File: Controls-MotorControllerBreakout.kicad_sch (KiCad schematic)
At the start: 15 parts, among them J1 MC CAN 1, J2 MC CAN 2, J3 CAN INTRFC, J4 EXT PWR

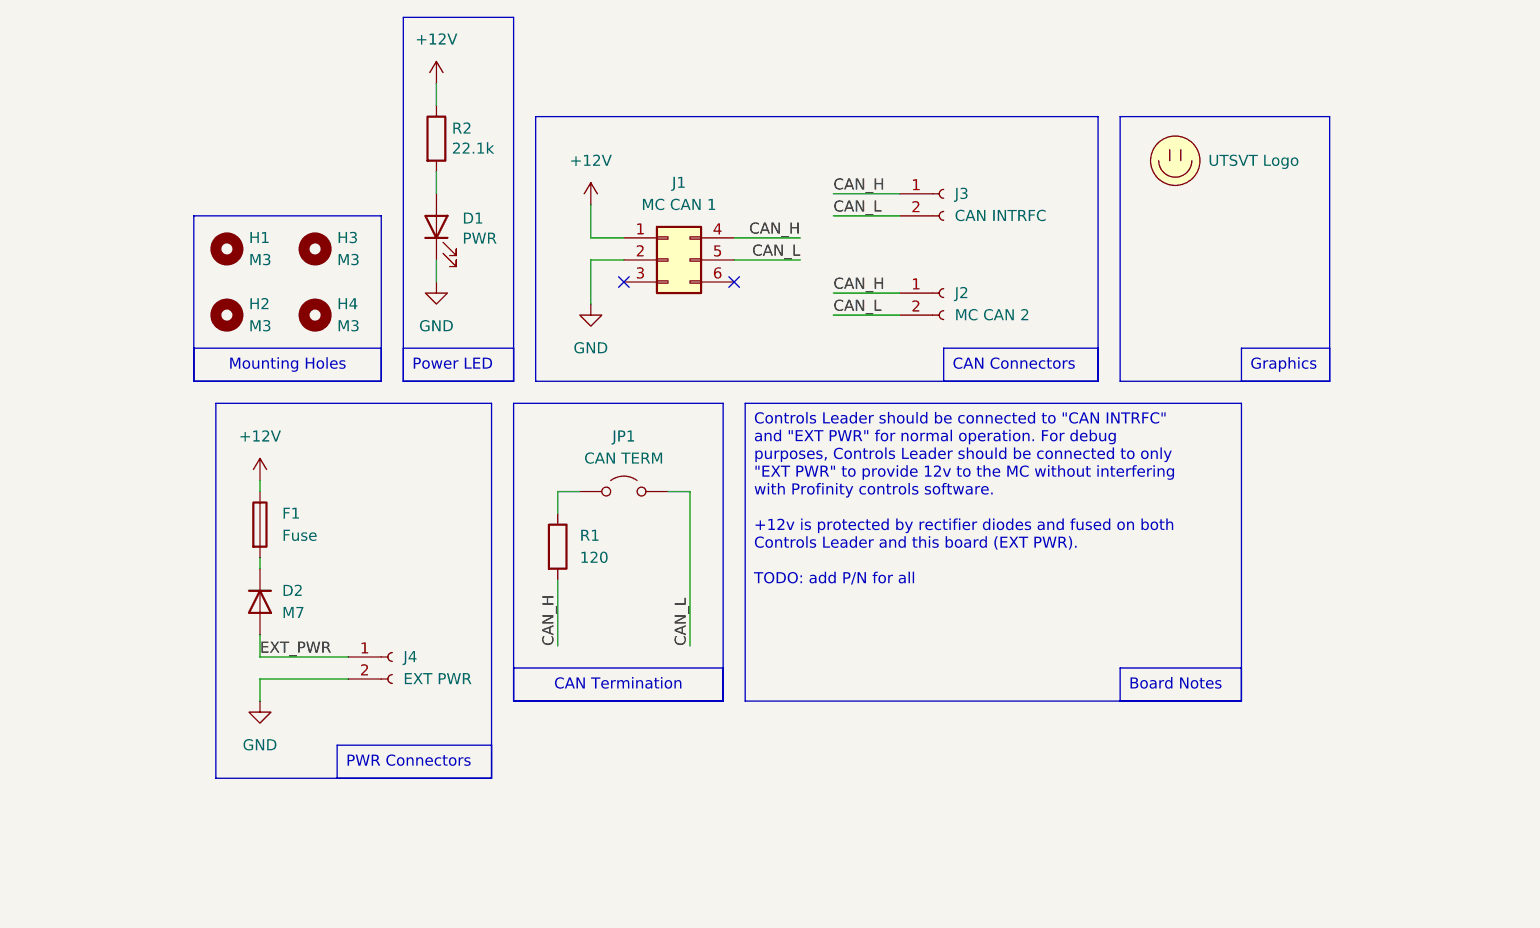
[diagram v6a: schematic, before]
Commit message: fix PP & add dsub conn
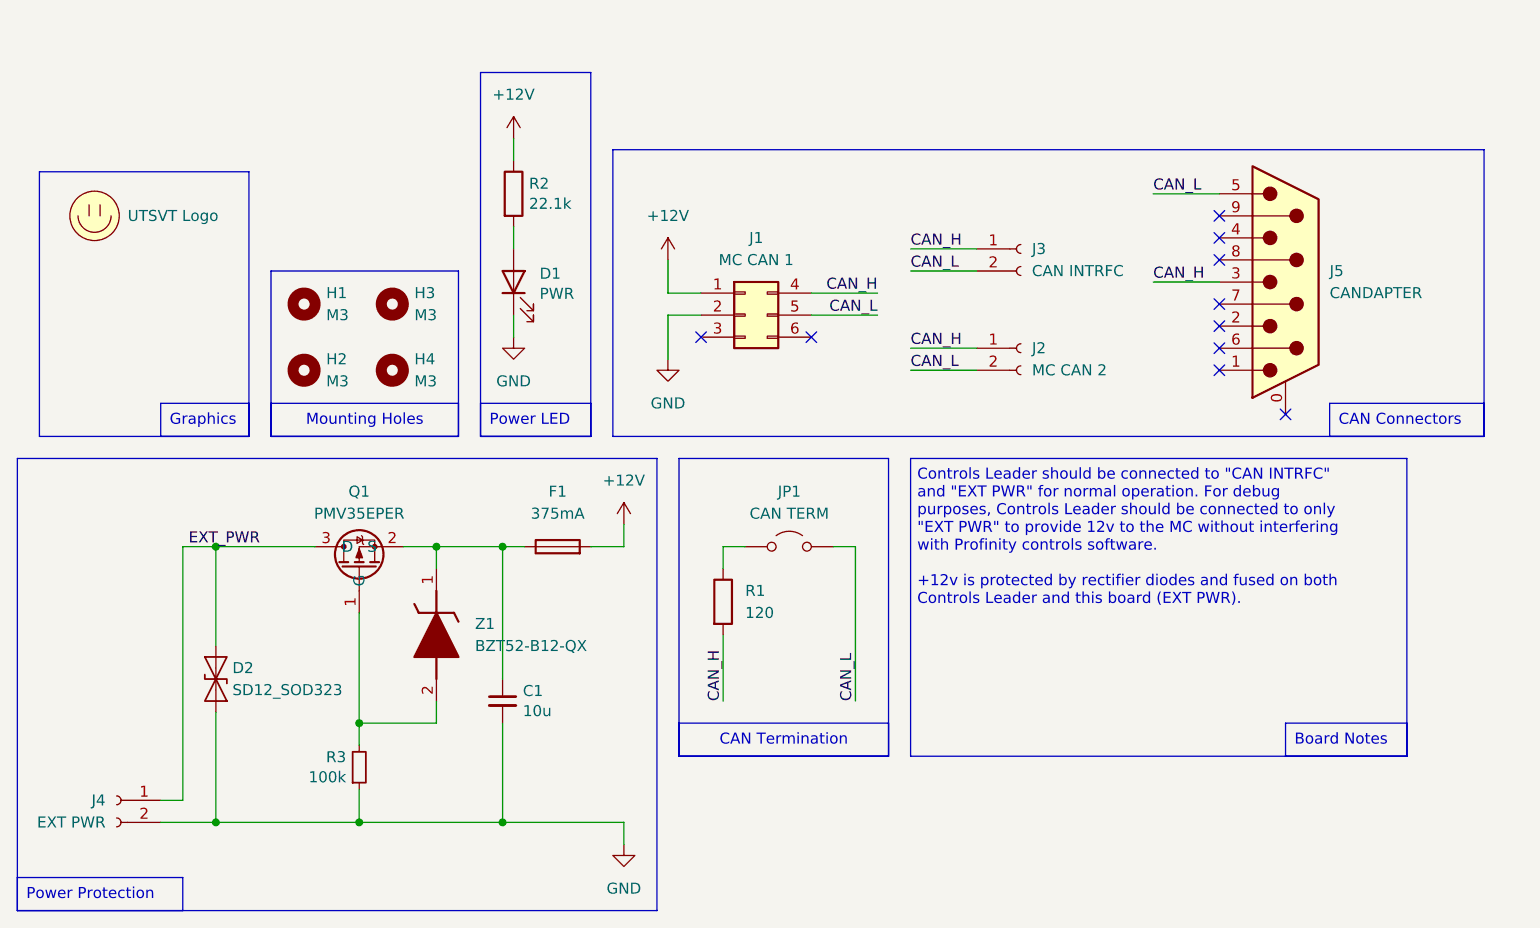
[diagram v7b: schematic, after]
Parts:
- removed D2: M7, Diode_SMD:D_SOD-123F, symbol Device:D
- added C1: 10u, Capacitor_SMD:C_0805_2012Metric, symbol Device:C_Small
- added D2: SD12_SOD323, Diode_SMD:D_SOD-323, symbol Diode:SD12_SOD323
- added J5: CANDAPTER, DB-9 Connector:AMPHENOL_L77SDE09SA4CH3R, symbol Connector:DE9_Plug_MountingHoles
- added Q1: PMV35EPER, Package_TO_SOT_SMD:SOT-23, symbol utsvt-chips:PMV35EPE
- added R3: 100k, Resistor_SMD:R_0805_2012Metric_Pad1.20x1.40mm_HandSolder, symbol Device:R_Small
- added Z1: BZT52-B12-QX, Zener:BZT52B12QX, symbol BZT52-B12-QX:BZT52-B12-QX
- F1: value Fuse -> 375mA
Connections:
- net +12V: now also F1.2; no longer F1.1
- net CAN_H: now also J5.3
- net CAN_L: now also J5.5
- net EXT_PWR: now also D2.2 (A2), Q1.3 (D)
- net GND: now also C1.2, D2.1 (A1), R3.1
- new net: Q1.1 (G), R3.2, Z1.2 (A)
- new net: C1.1, F1.1, Q1.2 (S), Z1.1 (K)
- no-connect marks 2 -> 10
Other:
- note added: "Controls Leader should be connected to "CAN INTRFC" and "EXT PWR" for normal operation. For debug purposes, Controls Leader should be connected to only "EXT PWR" to provide 12v to the MC without interfering with Profinity controls software. +12v is protected by rectifier diodes and fused on both Controls Leader and this board (EXT PWR)."
- note removed: "Controls Leader should be connected to "CAN INTRFC" and "EXT PWR" for normal operation. For debug purposes, Controls Leader should be connected to only "EXT PWR" to provide 12v to the MC without interfering with Profinity controls software. +12v is protected by rectifier diodes and fused on both Controls Leader and this board (EXT PWR). TODO: add P/N for all"
- moved on the sheet: D1, H1, H2, H3, H4, J1, J2, J3, J4, JP1, R1, R2

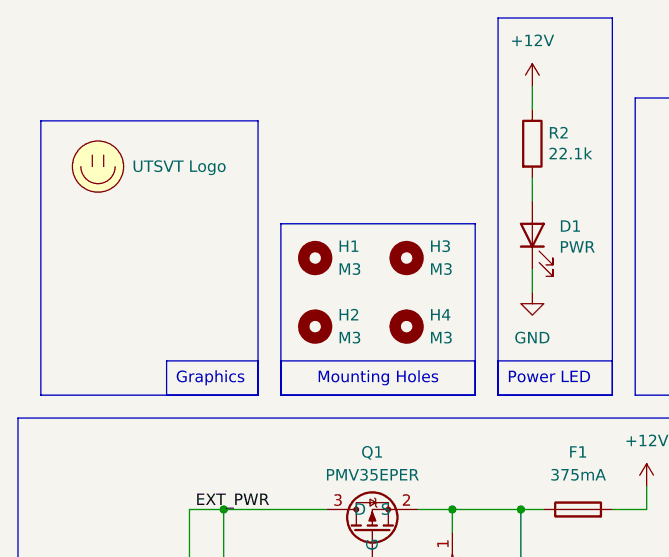
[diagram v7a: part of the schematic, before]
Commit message: rm mountingholes
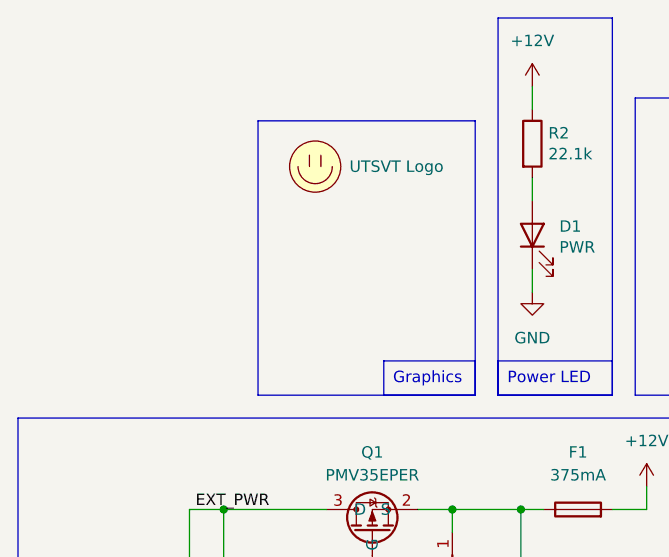
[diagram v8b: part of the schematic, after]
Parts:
- removed H1, H2, H3, H4: M3, MountingHole:MountingHole_3mm, symbol Mechanical:MountingHole
